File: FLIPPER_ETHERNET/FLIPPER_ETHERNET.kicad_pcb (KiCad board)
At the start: 2 copper layers, 67 x 25 mm, 38 parts, among them J1 RJ45_Hanrun_HR911105A_Horizon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, J2 Conn_01x08_Socket, J3 Conn_01x10_Socket, SW1 SW_Push, U1 ENC28J60x-ML, Y1 25MHz

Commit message: feat: some pcb routes corrected
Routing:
- net +3.3V: track 75.8 -> 80.4 mm
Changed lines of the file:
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@@
-	)
-	(segment
-		(start 150.63 62.555)
-		(end 150.63 66.72)
-		(width 0.3)
-		(layer "B.Cu")
-		(net 6)
 	)
 	(segment
@@
 	)
 	(segment
+		(start 150.63 66.4)
+		(end 150.31 66.72)
+		(width 0.2)
+		(layer "B.Cu")
+		(net 6)
+	)
+	(segment
+		(start 148.43 66.4)
+		(end 148.75 66.72)
+		(width 0.2)
+		(layer "B.Cu")
+		(net 6)
+	)
+	(segment
+		(start 148.43 66.4)
+		(end 148.43 66.72)
+		(width 0.3)
+		(layer "B.Cu")
+		(net 6)
+	)
+	(segment
 		(start 145.495 49.955)
 		(end 145.48 49.94)
@@
 	)
 	(segment
-		(start 154.1 62.5)
-		(end 154.1 66.72)
-		(width 0.3)
-		(layer "B.Cu")
-		(net 6)
-	)
-	(segment
 		(start 155.82 67.16)
 		(end 155.82 68.27)
@@
 	)
 	(segment
-		(start 139.49 62.565)
-		(end 139.49 66.72)
-		(width 0.3)
-		(layer "B.Cu")
-		(net 6)
-	)
-	(segment
-		(start 148.43 62.555)
-		(end 148.43 66.72)
-		(width 0.3)
+		(start 154.1 66.4)
+		(end 154.42 66.72)
+		(width 0.2)
 		(layer "B.Cu")
 		(net 6)
@@
 	)
 	(segment
+		(start 154.1 66.4)
+		(end 153.78 66.72)
+		(width 0.2)
+		(layer "B.Cu")
+		(net 6)
+	)
+	(segment
+		(start 135.45 57.04)
+		(end 135.45 57.39)
+		(width 0.3)
+		(layer "B.Cu")
+		(net 6)
+	)
+	(segment
+		(start 148.43 62.555)
+		(end 148.43 66.4)
+		(width 0.3)
+		(layer "B.Cu")
+		(net 6)
+	)
+	(segment
+		(start 148.43 66.4)
+		(end 148.11 66.72)
+		(width 0.2)
+		(layer "B.Cu")
+		(net 6)
+	)
+	(segment
 		(start 135.45 65.98)
 		(end 136.19 66.72)
@@
 	)
 	(segment
-		(start 154.1 66.72)
-		(end 155.38 66.72)
-		(width 0.3)
-		(layer "B.Cu")
-		(net 6)
-	)
-	(segment
-		(start 148.43 66.72)
-		(end 150.63 66.72)
+		(start 139.49 66.4)
+		(end 139.17 66.72)
+		(width 0.2)
+		(layer "B.Cu")
+		(net 6)
+	)
+	(segment
+		(start 139.49 66.4)
+		(end 139.49 66.72)
 		(width 0.3)
 		(layer "B.Cu")
@@
 	)
 	(segment
-		(start 136.19 66.72)
-		(end 139.49 66.72)
+		(start 139.81 66.72)
+		(end 148.11 66.72)
+		(width 0.3)
+		(layer "B.Cu")
+		(net 6)
+	)
+	(segment
+		(start 154.42 66.72)
+		(end 155.38 66.72)
+		(width 0.3)
+		(layer "B.Cu")
+		(net 6)
+	)
+	(segment
+		(start 148.11 66.72)
+		(end 148.43 66.72)
 		(width 0.3)
 		(layer "B.Cu")
@@
 	)
 	(segment
+		(start 150.63 66.72)
+		(end 150.95 66.72)
+		(width 0.3)
+		(layer "B.Cu")
+		(net 6)
+	)
+	(segment
 		(start 146.67 49.955)
 		(end 145.495 49.955)
@@
 	)
 	(segment
+		(start 135.8 57.04)
+		(end 135.45 57.04)
+		(width 0.3)
+		(layer "B.Cu")
+		(net 6)
+	)
+	(segment
+		(start 150.63 66.4)
+		(end 150.63 66.72)
+		(width 0.3)
+		(layer "B.Cu")
+		(net 6)
+	)
+	(segment
+		(start 153.78 66.72)
+		(end 154.1 66.72)
+		(width 0.3)
+		(layer "B.Cu")
+		(net 6)
+	)
+	(segment
+		(start 150.31 66.72)
+		(end 150.63 66.72)
+		(width 0.3)
+		(layer "B.Cu")
+		(net 6)
+	)
+	(segment
+		(start 150.63 66.4)
+		(end 150.95 66.72)
+		(width 0.2)
+		(layer "B.Cu")
+		(net 6)
+	)
+	(segment
+		(start 139.49 62.565)
+		(end 139.49 66.4)
+		(width 0.3)
+		(layer "B.Cu")
+		(net 6)
+	)
+	(segment
+		(start 148.43 66.72)
+		(end 148.75 66.72)
+		(width 0.3)
+		(layer "B.Cu")
+		(net 6)
+	)
+	(segment
+		(start 154.1 66.4)
+		(end 154.1 66.72)
+		(width 0.3)
+		(layer "B.Cu")
+		(net 6)
+	)
+	(segment
+		(start 135.8 57.04)
+		(end 135.45 56.69)
+		(width 0.2)
+		(layer "B.Cu")
+		(net 6)
+	)
+	(segment
+		(start 135.8 57.04)
+		(end 135.45 57.39)
+		(width 0.2)
+		(layer "B.Cu")
+		(net 6)
+	)
+	(segment
+		(start 135.45 56.69)
+		(end 135.45 57.04)
+		(width 0.3)
+		(layer "B.Cu")
+		(net 6)
+	)
+	(segment
+		(start 135.45 52.67)
+		(end 135.45 56.69)
+		(width 0.3)
+		(layer "B.Cu")
+		(net 6)
+	)
+	(segment
+		(start 150.63 62.555)
+		(end 150.63 66.4)
+		(width 0.3)
+		(layer "B.Cu")
+		(net 6)
+	)
+	(segment
+		(start 135.45 57.39)
+		(end 135.45 65.98)
+		(width 0.3)
+		(layer "B.Cu")
+		(net 6)
+	)
+	(segment
+		(start 148.75 66.72)
+		(end 150.31 66.72)
+		(width 0.3)
+		(layer "B.Cu")
+		(net 6)
+	)
+	(segment
 		(start 138.755 57.04)
-		(end 135.45 57.04)
-		(width 0.3)
-		(layer "B.Cu")
-		(net 6)
-	)
-	(segment
-		(start 150.63 66.72)
-		(end 154.1 66.72)
-		(width 0.3)
-		(layer "B.Cu")
-		(net 6)
-	)
-	(segment
-		(start 135.45 57.04)
-		(end 135.45 65.98)
+		(end 135.8 57.04)
+		(width 0.3)
+		(layer "B.Cu")
+		(net 6)
+	)
+	(segment
+		(start 154.1 62.5)
+		(end 154.1 66.4)
 		(width 0.3)
 		(layer "B.Cu")
@@
 	(segment
 		(start 139.49 66.72)
-		(end 148.43 66.72)
-		(width 0.3)
-		(layer "B.Cu")
-		(net 6)
-	)
-	(segment
-		(start 135.45 52.67)
-		(end 135.45 57.04)
-		(width 0.3)
-		(layer "B.Cu")
+		(end 139.81 66.72)
+		(width 0.3)
+		(layer "B.Cu")
+		(net 6)
+	)
+	(segment
+		(start 139.49 66.4)
+		(end 139.81 66.72)
+		(width 0.2)
+		(layer "B.Cu")
+		(net 6)
+	)
+	(segment
+		(start 154.1 66.72)
+		(end 154.42 66.72)
+		(width 0.3)
+		(layer "B.Cu")
+		(net 6)
+	)
+	(segment
+		(start 139.17 66.72)
+		(end 139.49 66.72)
+		(width 0.3)
+		(layer "B.Cu")
+		(net 6)
+	)
+	(segment
+		(start 150.95 66.72)
+		(end 153.78 66.72)
+		(width 0.3)
+		(layer "B.Cu")
+		(net 6)
+	)
+	(segment
+		(start 136.19 66.72)
+		(end 139.17 66.72)
+		(width 0.3)
+		(layer "B.Cu")

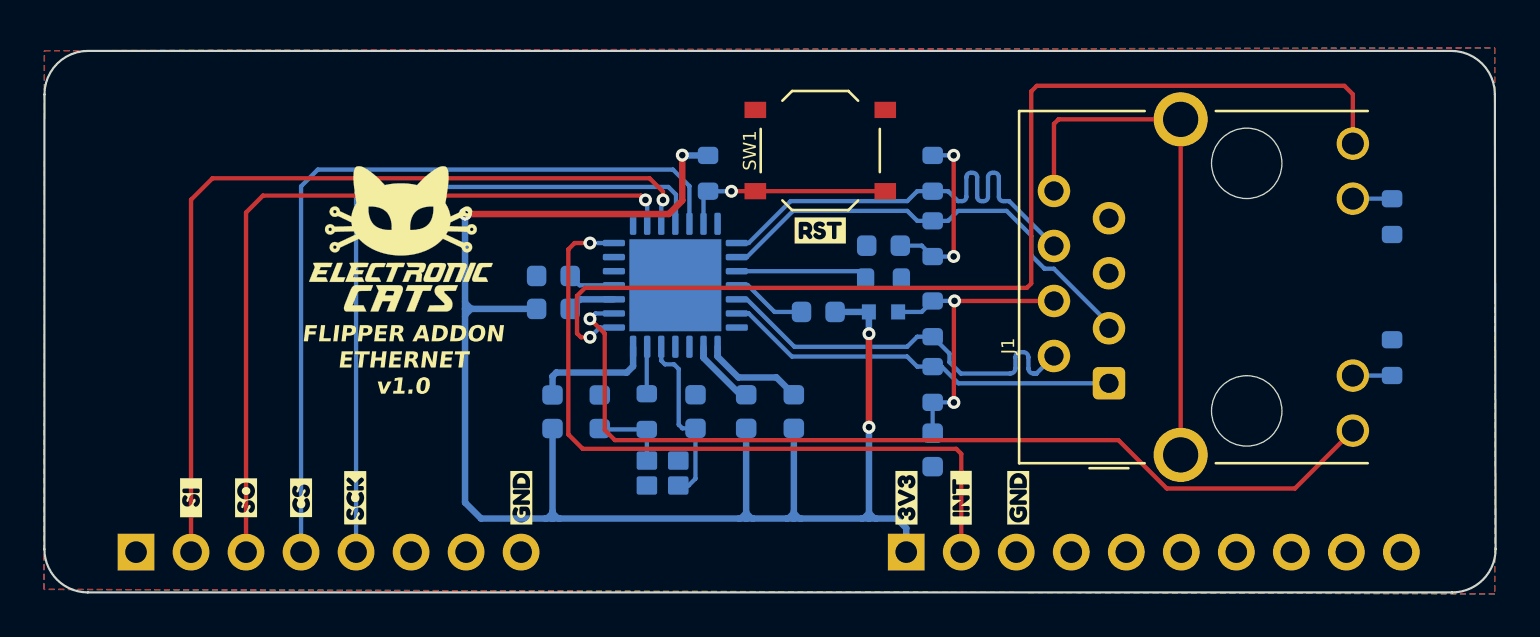
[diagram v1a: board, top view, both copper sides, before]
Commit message: feat: flipper ethernet pcb modified
decoupling capacitor connections fixed

components moved close to the ethernet

differential pairs and other routes modified
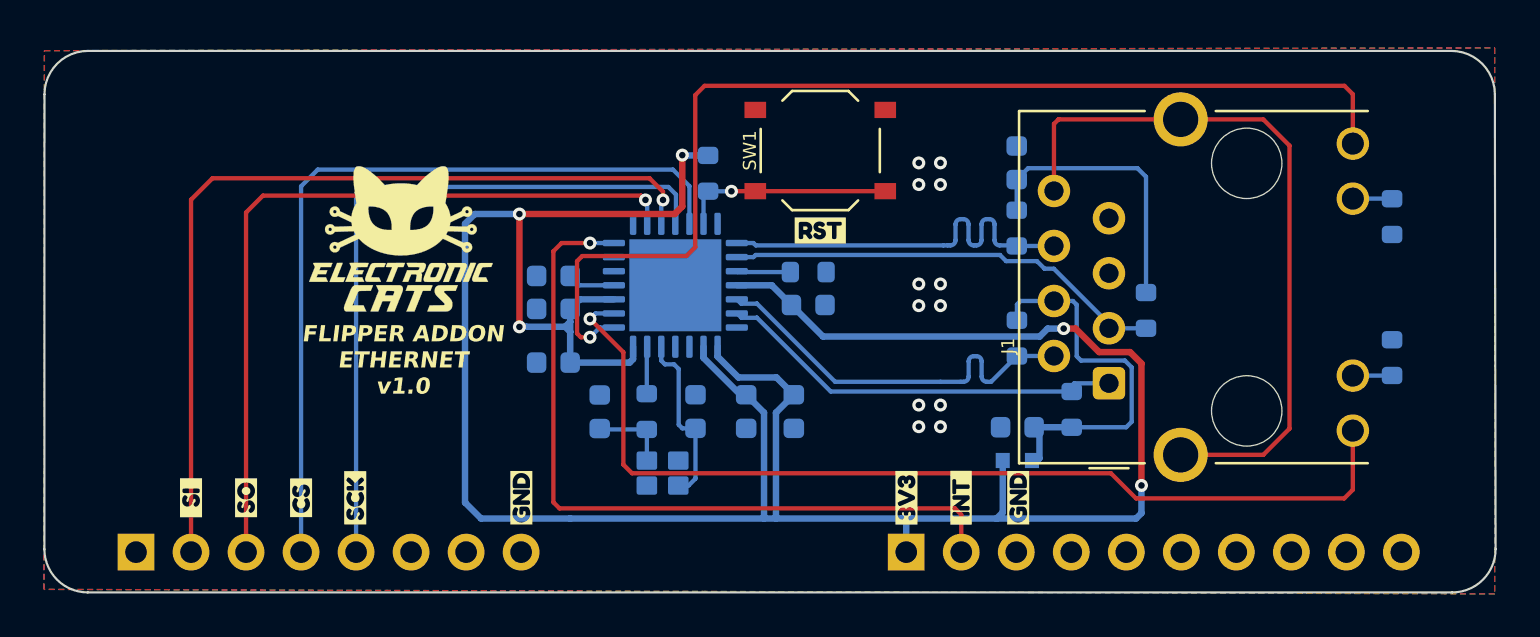
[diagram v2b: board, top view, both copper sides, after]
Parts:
- moved R7 10.4 mm to (166.9, 57.1), turned to 90 degrees
- moved FB1 9.23 mm to (160.9, 64.0)
- moved C3 7.24 mm to (160.9, 50.3), turned to 90 degrees
- moved R5 6.52 mm to (163.5, 61.7)
- moved R8 4.63 mm to (160.9, 53.3)
- moved C4 4.05 mm to (160.9, 62.5), turned to 180 degrees
- moved R6 3.99 mm to (160.9, 58.4)
- moved R9 3.49 mm to (151.3, 55.3)
- moved C10 2.27 mm to (139.5, 59.5), turned to 0 degrees
- moved C6 0.56 mm to (151.3, 56.9)
- turned C9 to 90 degrees
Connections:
- C10 pad 1: +3.3V -> GND
- C10 pad 2: Net-(U1-VDDOSC) -> +3.3V
- C6 pad 1: Net-(U1-VDDTX) -> +3.3V
- C6 pad 2: +3.3V -> GND
- C7 pad 1: Net-(U1-VDDRX) -> +3.3V
- C7 pad 2: +3.3V -> GND
- C8 pad 1: +3.3V -> GND
- C8 pad 2: Net-(U1-VDD) -> +3.3V
- C9 pad 1: Net-(U1-VDDPLL) -> GND
- U1 pad 11: Net-(U1-VDDTX) -> +3.3V
- U1 pad 15: Net-(U1-VDDRX) -> +3.3V
- U1 pad 16: Net-(U1-VDDPLL) -> +3.3V
- U1 pad 21: Net-(U1-VDDOSC) -> +3.3V
- U1 pad 24: Net-(U1-VDD) -> +3.3V
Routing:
- net +3.3V: track 80.4 -> 126.8 mm, vias 4 -> 5
- net Net-(J1-Pad8): track 24.5 -> 33.2 mm
- net Net-(U1-VDDOSC): track 5.68 -> 0.00 mm
- net Net-(C3-Pad1): track 8.32 -> 13.1 mm, vias 2 -> 0
- net Net-(U1-VDDRX): track 4.71 -> 0.00 mm
- net Net-(U1-RBIAS): track 6.09 -> 2.49 mm
- net Net-(U1-VDDTX): track 3.50 -> 0.00 mm
- net Net-(U1-VDDPLL): track 3.19 -> 0.00 mm
- net /TCT: track 14.5 -> 17.5 mm, vias 2 -> 0
- net /RD-: track 21.2 -> 18.7 mm
- net /LEDA: track 43.4 -> 45.8 mm
- net Net-(U1-VDD): track 2.20 -> 0.00 mm
- net /INT: track 33.8 -> 35.3 mm
- net /RD+: track 21.4 -> 20.5 mm
- net GND: vias 0 -> 12

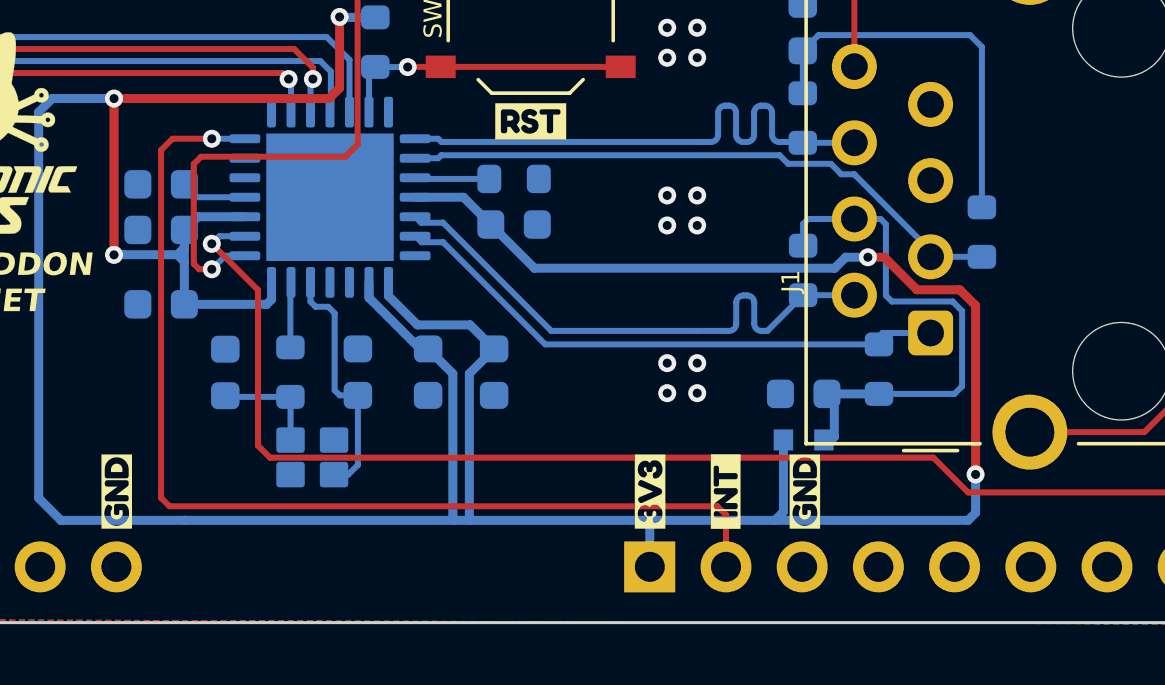
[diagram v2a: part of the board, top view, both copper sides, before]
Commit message: fix traces
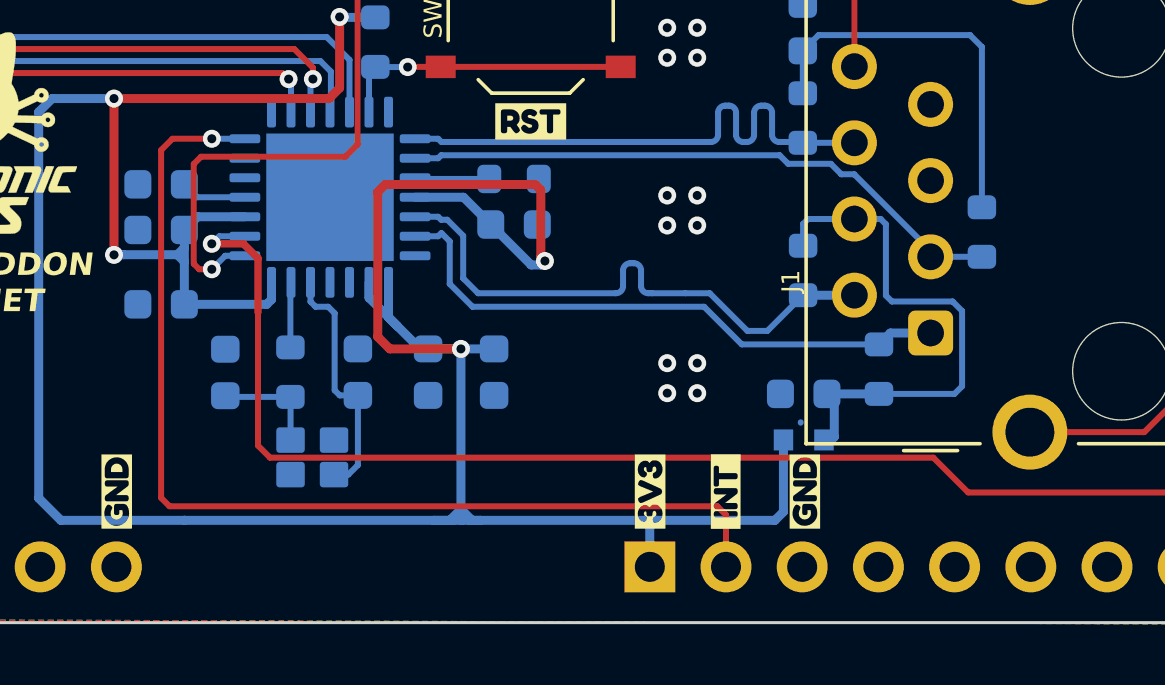
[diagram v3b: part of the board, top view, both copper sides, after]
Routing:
- net +3.3V: track 126.8 -> 108.3 mm
- net /TD+: track 19.0 -> 19.7 mm
- net /LEDA: track 45.8 -> 46.4 mm

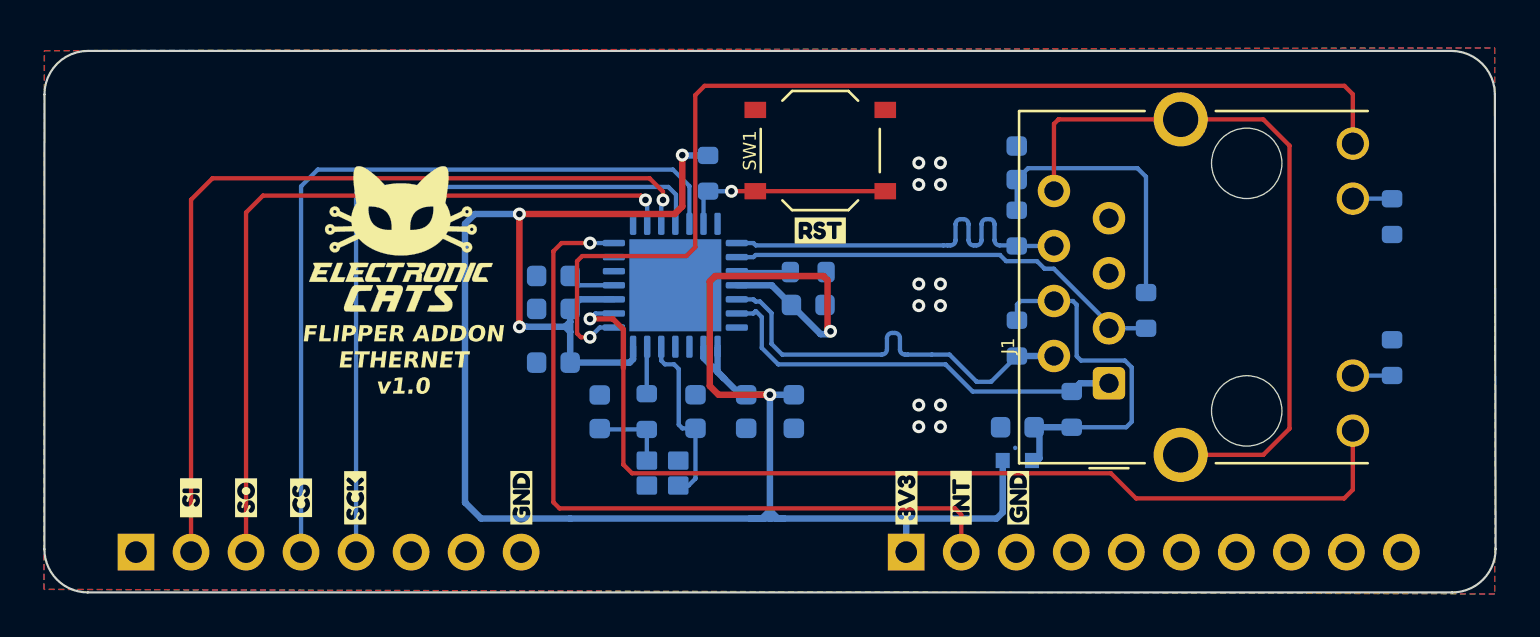
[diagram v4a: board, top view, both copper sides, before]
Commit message: feat(Hw): changed reset to flipper
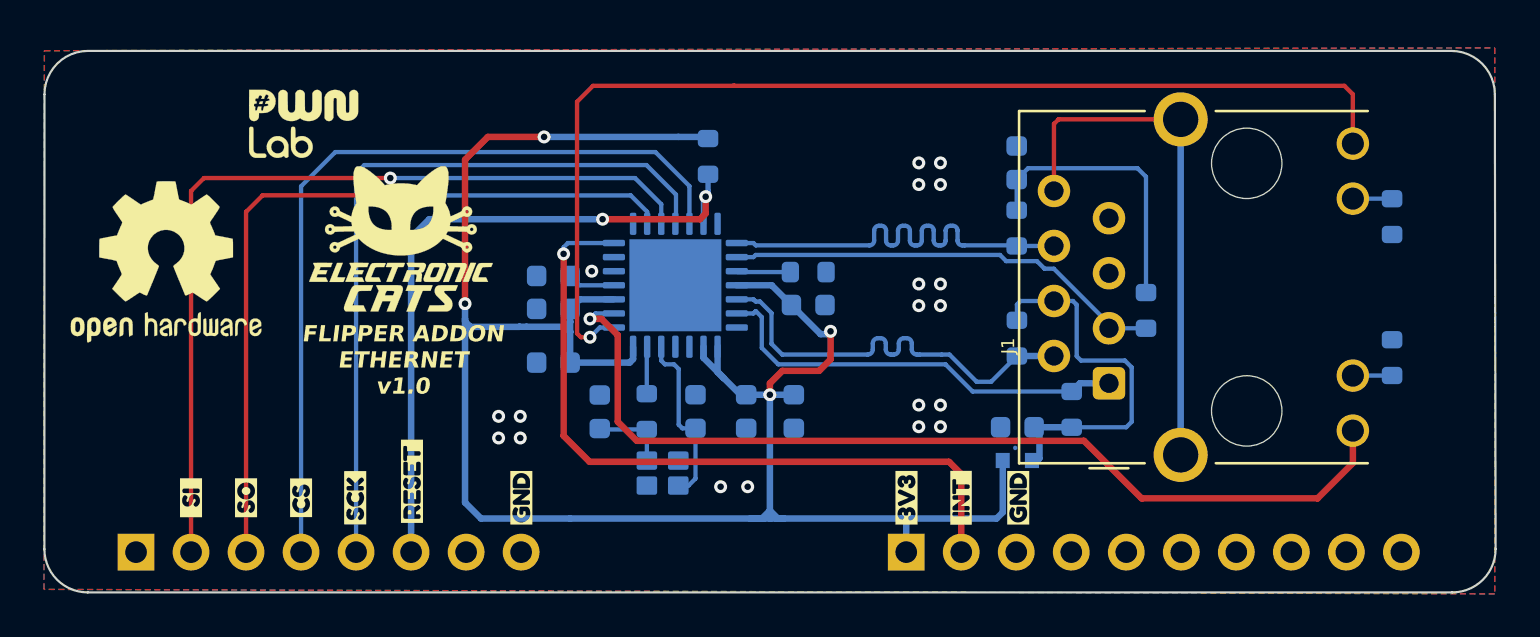
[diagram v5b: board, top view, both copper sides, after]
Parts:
- removed SW1: SW_Push, Button_Switch_SMD:SW_Push_1P1T_XKB_TS-1187A
- removed kibuzzard-67102A6B: G***, kibuzzard-67102A6B
- added G***: LOGO, CatSniffer:calderon, F.Cu at (128.0, 48.5)
- added kibuzzard-6835A348: G***, kibuzzard-6835A348, F.Cu at (133.0, 65.0)
- REF**: moved to F.Cu
- moved R2 0.78 mm to (146.7, 50.0)
- turned REF** to 0 degrees
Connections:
- J2 pad 6: unconnected-(J2-Pin_6-Pad6) -> /RESET
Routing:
- net /RESET: track 9.78 -> 31.7 mm, vias 1 -> 2
- net +3.3V: track 108.3 -> 96.6 mm, vias 5 -> 4
- net Net-(J1-Pad8): track 33.2 -> 24.5 mm
- net /LEDA: track 46.4 -> 44.4 mm
- net /RD-: track 18.7 -> 20.3 mm
- net /INT: track 35.3 -> 33.8 mm
- net /SCK: track 33.0 -> 34.3 mm
- net /CS: track 37.2 -> 37.9 mm
- net /TD-: track 19.1 -> 19.7 mm
- net GND: vias 12 -> 19
